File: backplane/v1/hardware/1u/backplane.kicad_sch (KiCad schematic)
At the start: 14 parts, among them J1 Conn_02x20_Odd_Even, J2 Conn_02x20_Odd_Even, J3 Conn_02x20_Odd_Even, J4 Conn_02x20_Odd_Even

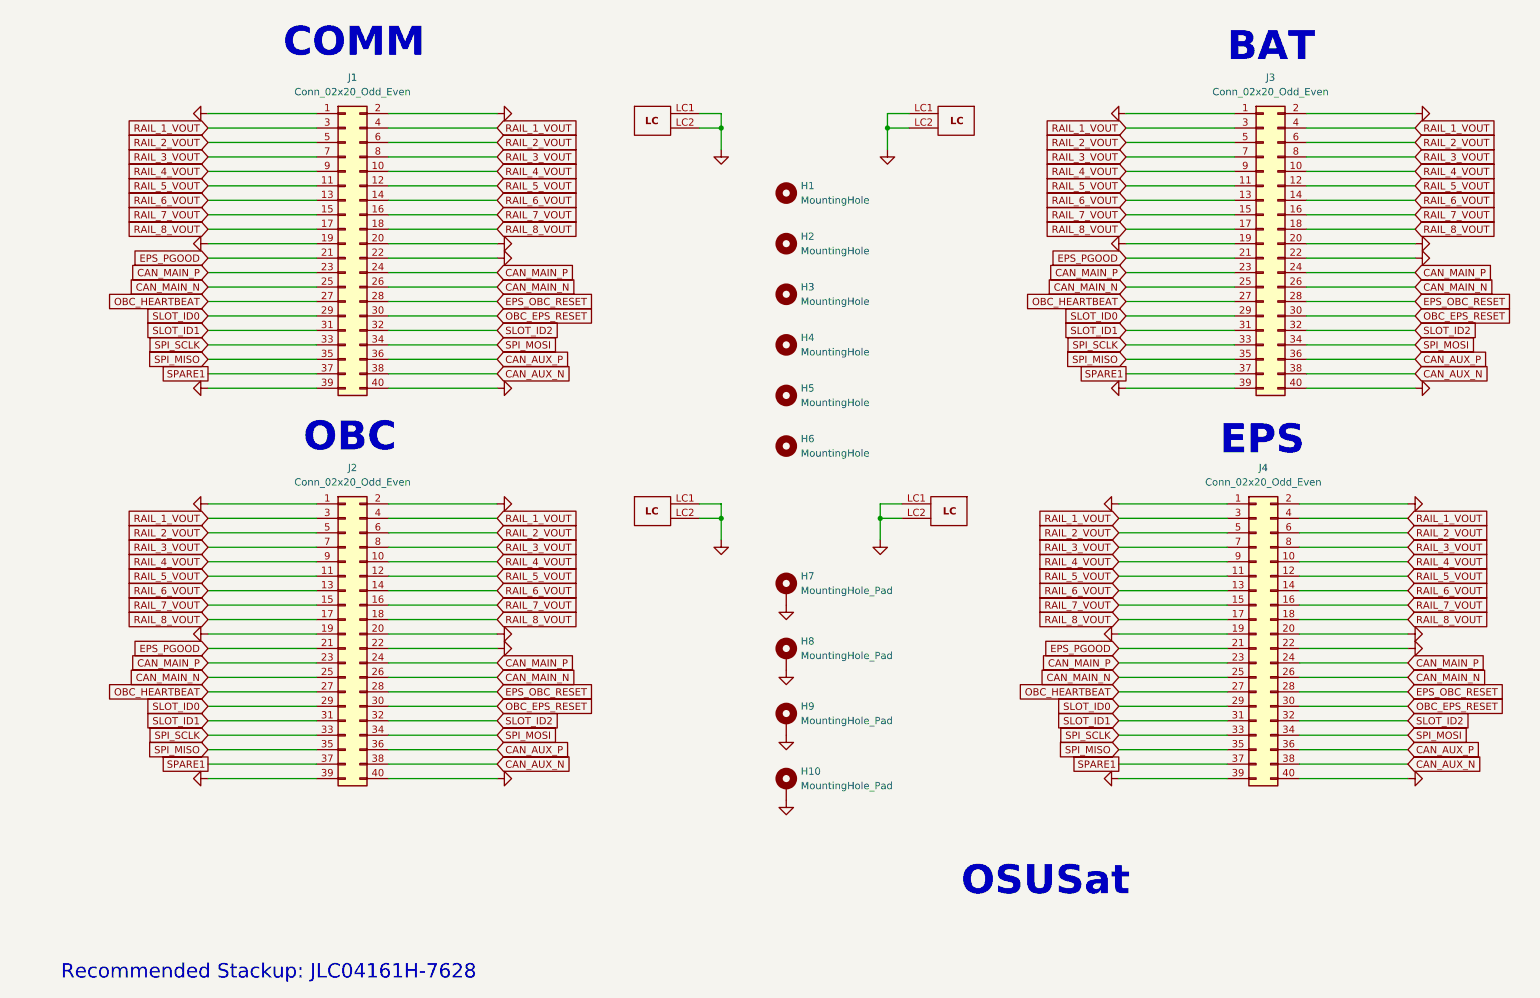
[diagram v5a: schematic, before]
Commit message: fix board clearance DRC & modify slot ID
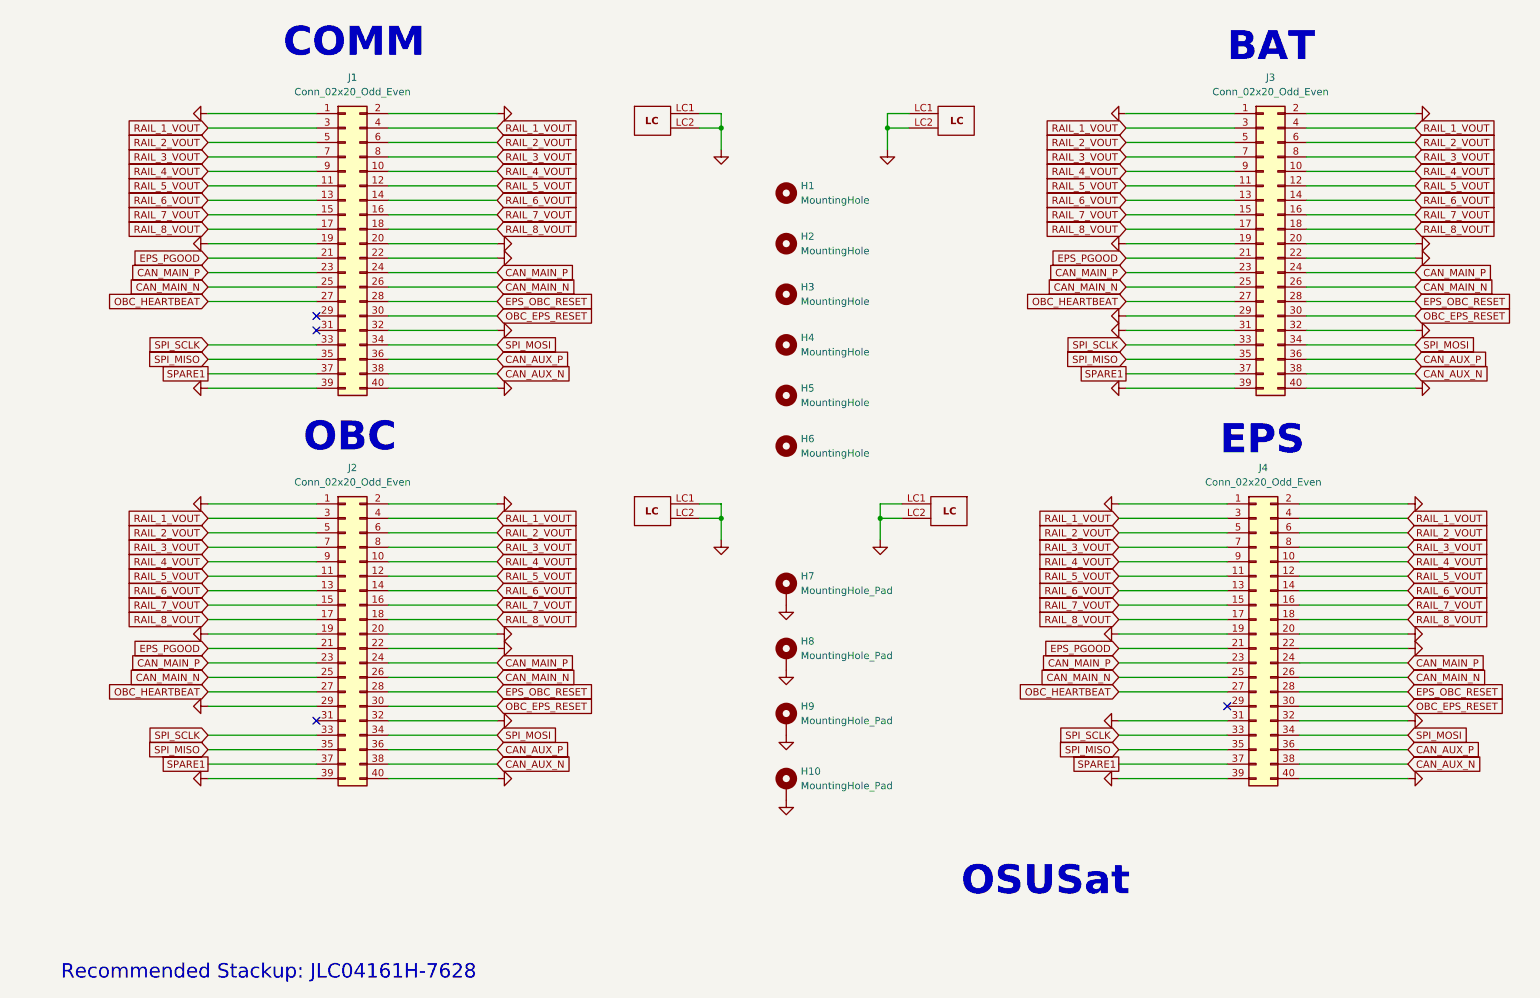
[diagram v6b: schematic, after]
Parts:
- J1, J2, J3, J4: footprint footprints:SFM-120-X1-XXX-D -> OSUSAT_Connectors:SFM-120-X1-XXX-D
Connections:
- net SLOT_ID2 is gone; now on net GND: J1.32 (Pin_32), J2.32 (Pin_32), J3.32 (Pin_32), J4.32 (Pin_32)
- net GND: now also J2.29 (Pin_29), J3.29 (Pin_29), J3.31 (Pin_31), J4.31 (Pin_31)
- removed net SLOT_ID0: J1.29 (Pin_29), J2.29 (Pin_29), J3.29 (Pin_29), J4.29 (Pin_29)
- removed net SLOT_ID1: J1.31 (Pin_31), J2.31 (Pin_31), J3.31 (Pin_31), J4.31 (Pin_31)
- no-connect marks 0 -> 4
